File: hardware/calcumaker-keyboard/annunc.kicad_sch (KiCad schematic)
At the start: 10 parts

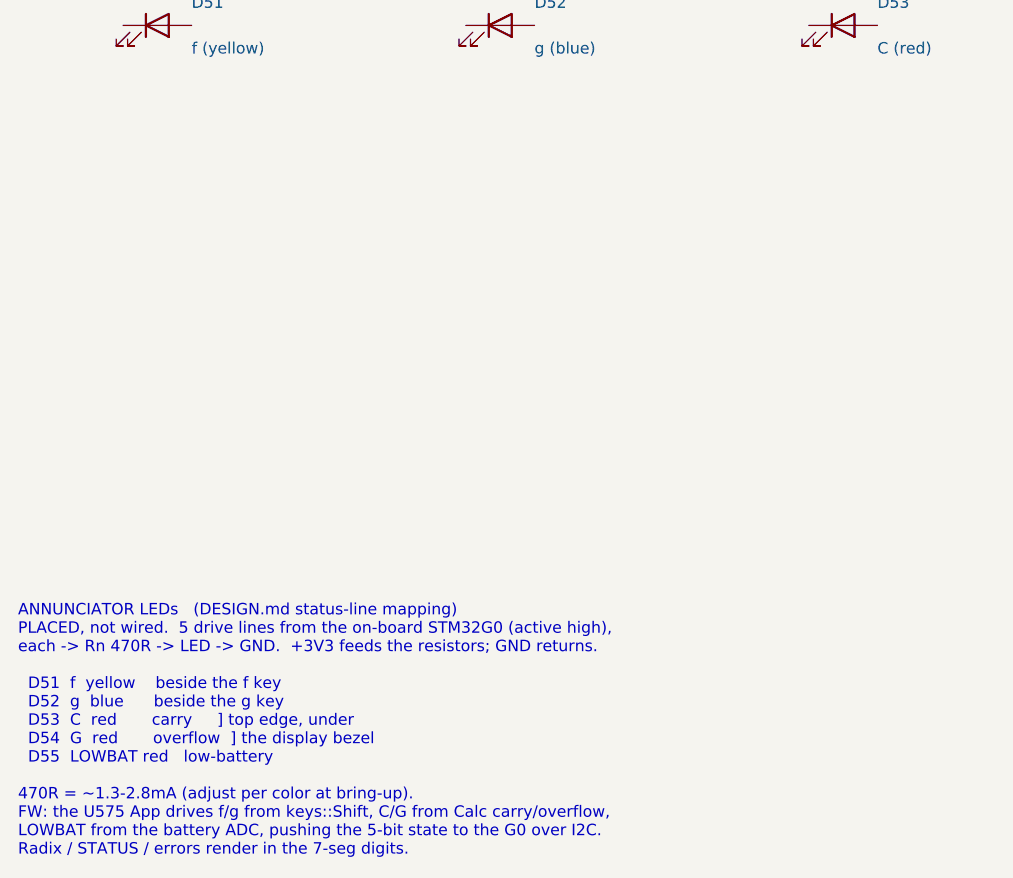
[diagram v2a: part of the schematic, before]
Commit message: hardware: per-key RGB hint lighting on the keyboard board (50x SK6805 on gated VSYS) (#4)
Add addressable RGB accent lighting that hints key positions / presses -- one
SK6805-EC15 (1.5x1.5mm, the smallest serial RGB with a KiCad footprint + real
LCSC stock, C2890035) beside each of the 50 keys, single-wire daisy chain off
one STM32G0 pin.

Power: the LEDs are ~5V parts and the keyboard rail is only 3.3V, so they run
off VSYS (the MCU board's load-shared battery/USB rail, ~3.7-4.7V) brought up a
WIDENED 12-pin mezzanine (10 -> 12: +VSYS +GND). A high-side P-FET load switch
(Q1 AO3401A + Q2 2N7002) gates the whole LED rail off in sleep (G0 LED_EN) to
protect battery life, and a 74LVC1G125 (powered from the gated rail) level-shifts
the 3.3V data up to the LED VIH.

- calcumaker-keyboard: new KeyLighting sheet (50x SK6805 D56-D105 + U2 shifter +
  Q1/Q2 load switch + R7-R10 / C6-C7); J1 mezzanine -> 12-pin DF40C-12DP
  (C6224952). 119 -> 178 components.
- calcumaker-mcu: J5 mezzanine -> 12-pin DF40B-12DS (C3641147); route VSYS.
- DF40 stack: the receptacle SUFFIX sets the mated height (none = 1.5mm,
  (2.0) = 2.0mm, H-series = 2.5-4.0mm), NOT the B/C letter; the DF40C plug is the
  common header -- so DF40C-12DP x DF40B-12DS is a valid 1.5mm stack, same as the
  original 10-pin (DF40C-12DS just isn't LCSC-stocked).
- DESIGN.md / PARTS.md / memory: RGB subsystem, 12-pin pinout, BOM rows, the
  sleep-gate + current-cap notes (firmware must cap total brightness; 50x
  full-white ~0.75A would exceed the DF40 / VSYS budget).

All three boards regenerate + pass the structure check (mcu 55 / keyboard 178 /
display 60, no duplicate refs).

Co-authored-by: Claude Opus 4.8 (1M context) <noreply@anthropic.com>
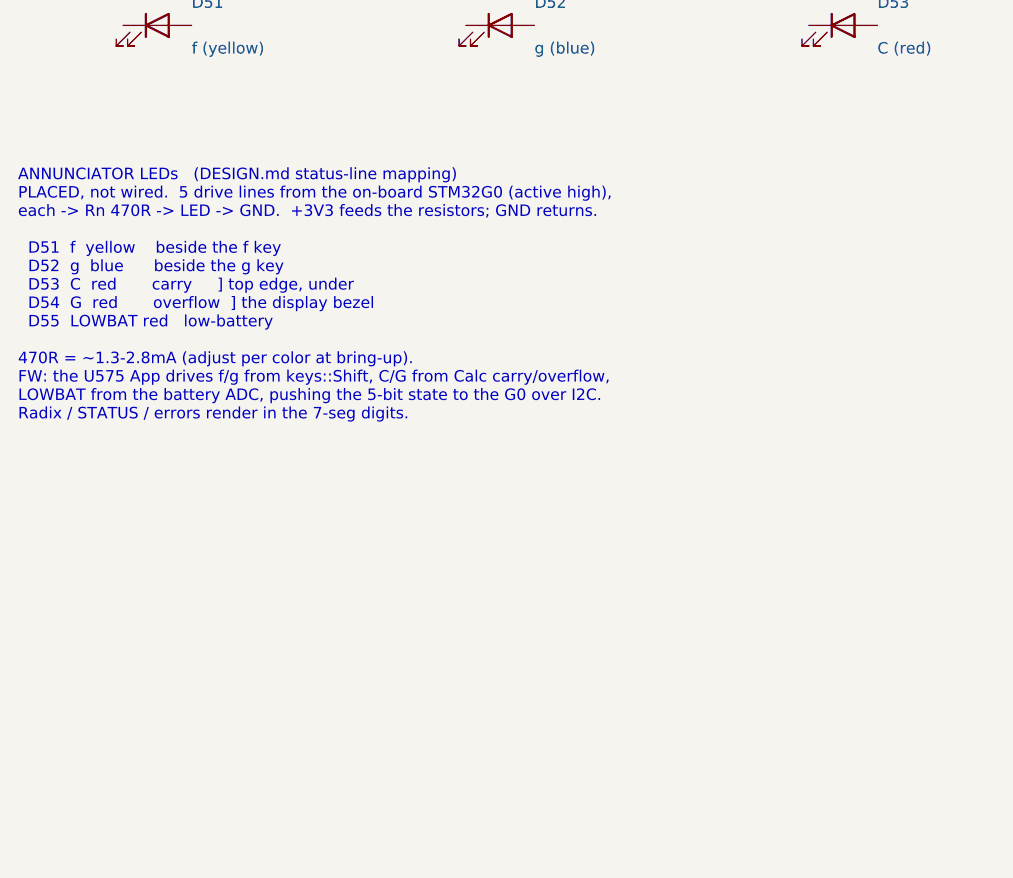
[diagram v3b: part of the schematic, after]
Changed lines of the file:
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@@
 	(title_block
 		(title "Calcumaker 16 — Keyboard — Annunciator LEDs (f g C G low-batt)")
-		(date "2026-07-05")
-		(rev "0.2")
+		(date "2026-07-06")
+		(rev "0.3")
 		(company "calcumaker authors")
 	)
@@
 	(text "ANNUNCIATOR LEDs   (DESIGN.md status-line mapping)\nPLACED, not wired.  5 drive lines from the on-board STM32G0 (active high),\neach -> Rn 470R -> LED -> GND.  +3V3 feeds the resistors; GND returns.\n\n  D51  f  yellow    beside the f key\n  D52  g  blue      beside the g key\n  D53  C  red       carry     ] top edge, under\n  D54  G  red       overflow  ] the display bezel\n  D55  LOWBAT red   low-battery\n\n470R = ~1.3-2.8mA (adjust per color at bring-up).\nFW: the U575 App drives f/g from keys::Shift, C/G from Calc carry/overflow,\nLOWBAT from the battery ADC, pushing the 5-bit state to the G0 over I2C.\nRadix / STATUS / errors render in the 7-seg digits."
 		(exclude_from_sim no)
-		(at 15.00 105.00 0)
+		(at 15.00 56.64 0)
 		(effects (font (face "Courier New") (size 1.27 1.27)) (justify left top))
 	)

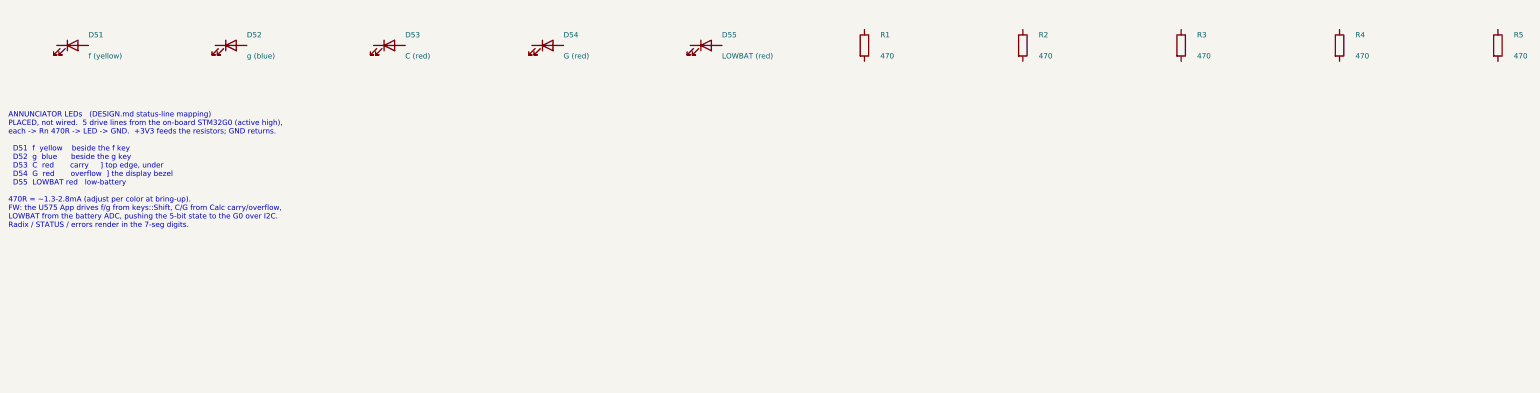
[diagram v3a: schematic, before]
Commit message: hardware: keyboard as a multi-channel design (reusable 10-key row x5) (#5)
Refactor calcumaker-keyboard from a FLAT layout (100 individually-placed SW/D
parts on one sheet + 50 flat RGB LEDs) into a KiCad multi-channel design,
matching the display board.

- key_row.kicad_sch: a reusable 10-key row, FULLY WIRED, instantiated x5
  (Row1-5). Each key = MX switch + 1N4148W diode + SK6805 RGB.
    matrix  SW.1 -> ROW (hier); SW.2 -> KNk -> diode.A; diode.K -> COLk (global)
    RGB     DIN -> LED1..LED10 -> DOUT (hier, chained @root); VDD->VLED, VSS->GND
  Per-instance refs SW1-50 / D1-50 (matrix) / D56-105 (RGB). Shared buses
  (COL1-10, VLED, GND) are global nets; ROW + RGB DIN/DOUT are hierarchical pins
  wired at the root (KB_ROW1-5; KB_LED_DATA -> Row1 -> ... -> Row5 -> RGB_END).
- Split the old KeyLighting sheet -> key_row (the 50 LEDs) + rgb_power (the
  level shifter + gated load switch).
- Converted the whole keyboard manifest from the flat K.build() path to the
  display-style write_wired_child/write_root API; the one-off sheets
  (annunc/kbd_mcu/rgb_power/main_if) stay single-instance, placed via a grid
  helper. Removed the obsolete keypad.kicad_sch + keylight.kicad_sch.
- Docs (DESIGN.md sheet plan, CLAUDE/AGENTS, scripts README) + a few stale fixes
  (STM32U575RGTx, "three boards", current sheet names).

178 components, no duplicate refs, all three boards pass the structure check.
(The 2 lib_symbol_mismatch ERC warnings on the G0/TagConnect are pre-existing
kschgen symbol-cache fidelity, not from this change.)

Co-authored-by: Claude Opus 4.8 (1M context) <noreply@anthropic.com>
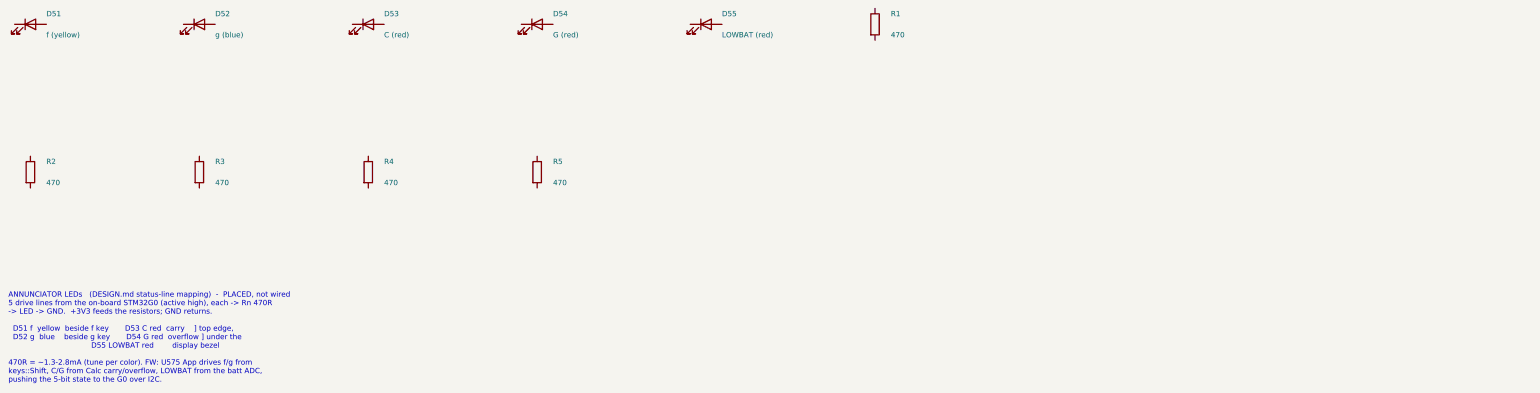
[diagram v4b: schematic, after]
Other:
- note added: "ANNUNCIATOR LEDs (DESIGN.md status-line mapping) - PLACED, not wired 5 drive lines from the on-board STM32G0 (active high), each -> Rn 470R -> LED -> GND. +3V3 feeds the resistors; GND returns. D51 f yellow beside f key D53 C red carry ] top edge, D52 g blue beside g key D54 G red overflow ] under the D55 LOWBAT red display bezel 470R = ~1.3-2.8mA (tune per color). FW: U575 App drives f/g from ke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"
- note removed: "ANNUNCIATOR LEDs (DESIGN.md status-line mapping) PLACED, not wired. 5 drive lines from the on-board STM32G0 (active high), each -> Rn 470R -> LED -> GND. +3V3 feeds the resistors; GND returns. D51 f yellow beside the f key D52 g blue beside the g key D53 C red carry ] top edge, under D54 G red overflow ] the display bezel D55 LOWBAT red low-battery 470R = ~1.3-2.8mA (adjust per color at bring-up)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"
